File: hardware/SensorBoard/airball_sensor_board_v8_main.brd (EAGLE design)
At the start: 5.6 x 9.2 mm, 56 parts, among them IC1 CP2102, J2 USB Female Type C Connector, T1 BC846, T2 BC846, U1 BQ24075, U2 BQ27441-G1, U3 BMP388, U4 ESP-WROOM-32, U7 SP0503BAHT

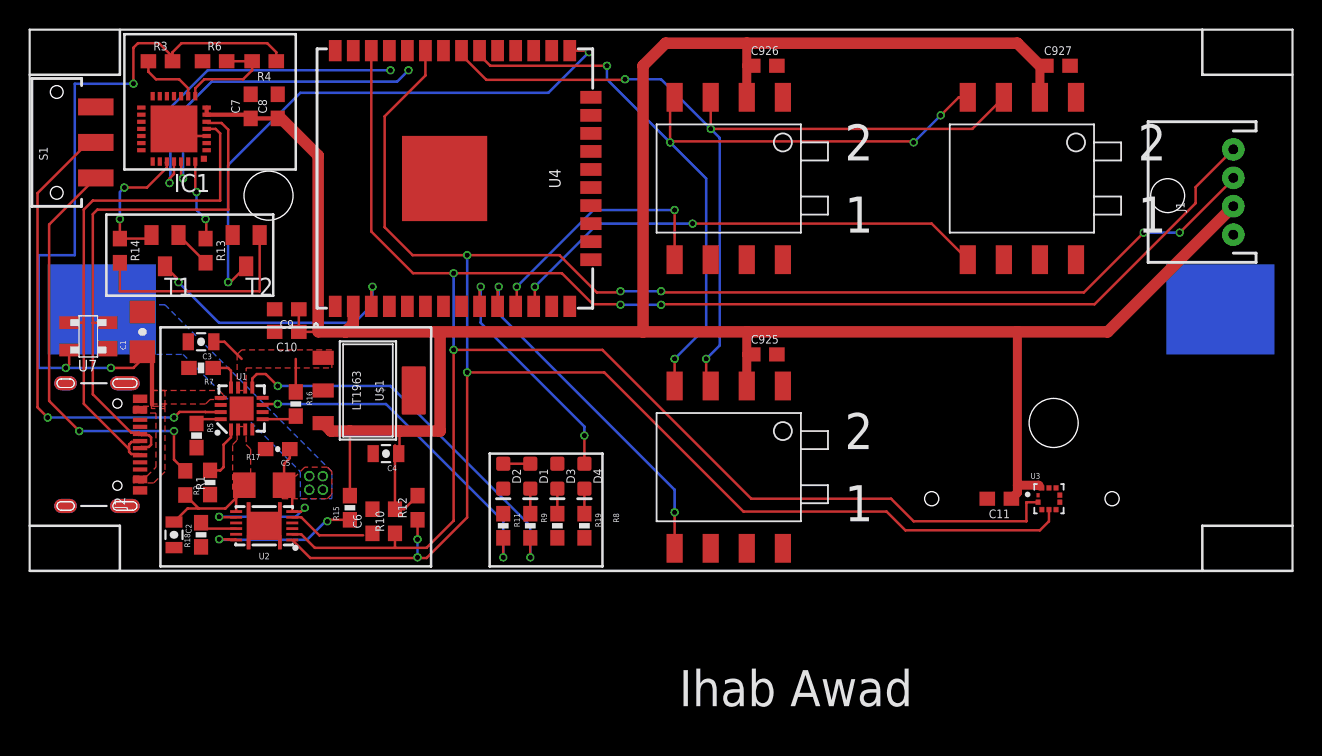
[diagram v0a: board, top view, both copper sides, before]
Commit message: More routing and documentation fixes.
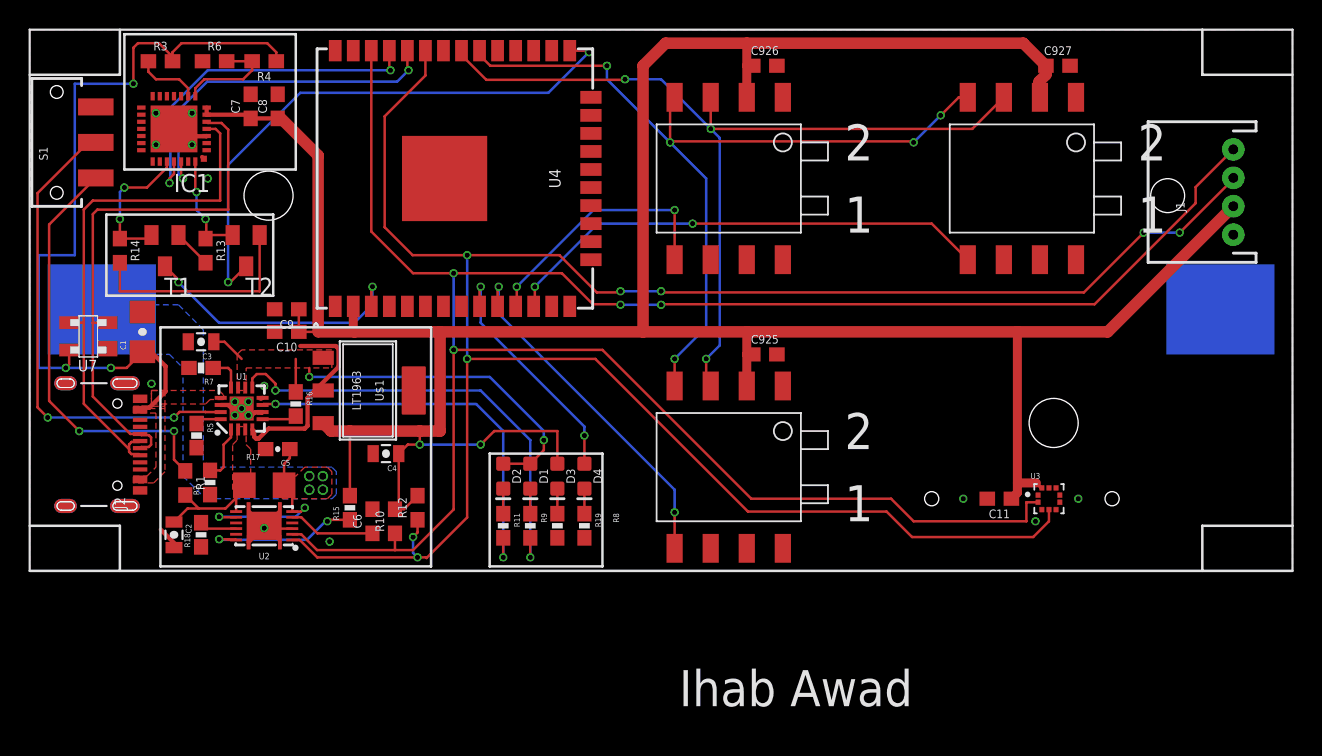
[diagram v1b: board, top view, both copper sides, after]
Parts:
- removed FRAME1, FRAME2: FRAME-LETTER, SparkFun-Aesthetics:CREATIVE_COMMONS
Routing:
- net GND: track 2.51 -> 34.5 mm, vias 0 -> 17
- net V_SUPPLY_UNREG: track 6.69 -> 28.1 mm, vias 0 -> 2
- net VCC: track 195.0 -> 209.0 mm, vias 0 -> 2
- net !CHG!: track 28.4 -> 32.2 mm
- net N$19: track 24.3 -> 28.0 mm
- net USB_TXD: track 23.1 -> 25.0 mm
- net N$20: track 0.00 -> 1.77 mm
- net USB_DTR: track 6.05 -> 7.70 mm
- net USB_RXD: track 23.6 -> 25.0 mm
- net SDA: track 160.5 -> 161.5 mm
- net N$14: track 5.52 -> 6.11 mm
- added copper zone on layer 1, net GND
- added copper zone on layer 16, net GND

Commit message: More routing fixes.
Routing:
- net GND: track 34.5 -> 19.6 mm
- net V_SUPPLY_UNREG: track 28.1 -> 29.2 mm, vias 2 -> 3
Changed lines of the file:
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@@
 <via x="14.9225" y="11.43" extent="1-16" drill="0.35"/>
 <via x="16.51" y="3.01625" extent="1-16" drill="0.35"/>
-<wire x1="16.3975" y1="11.18" x2="16.03095" y2="11.18" width="0.3048" layer="1"/>
 <via x="14.44625" y="11.90625" extent="1-16" drill="0.35"/>
 <via x="15.39875" y="11.90625" extent="1-16" drill="0.35"/>
@@
 <wire x1="15.639275" y1="10.95375" x2="15.39875" y2="10.95375" width="0.3048" layer="1"/>
 <wire x1="15.835725" y1="11.1502" x2="15.639275" y2="10.95375" width="0.3048" layer="1"/>
-<wire x1="14.9225" y1="11.43" x2="14.6427" y2="11.7098" width="0.3048" layer="1"/>
-<wire x1="14.009275" y1="11.6502" x2="14.705725" y2="10.95375" width="0.3048" layer="1"/>
 <wire x1="14.705725" y1="10.95375" x2="15.39875" y2="10.95375" width="0.3048" layer="1"/>
 <wire x1="10.542725" y1="1.5903" x2="9.2298" y2="2.903225" width="0.3048" layer="1"/>
@@
 <wire x1="16.3841" y1="12.1666" x2="16.2914" y2="12.1666" width="0.3048" layer="1"/>
 <wire x1="16.2914" y1="12.1666" x2="16.275" y2="12.1502" width="0.3048" layer="1"/>
-<wire x1="16.275" y1="12.1502" x2="16.1925" y2="12.1502" width="0.3048" layer="1"/>
 <via x="16.51" y="13.0175" extent="1-16" drill="0.35"/>
 <wire x1="15.41" y1="2.025" x2="16.430625" y2="3.045625" width="0.3048" layer="1"/>
 <wire x1="16.430625" y1="3.045625" x2="16.430625" y2="3.254375" width="0.3048" layer="1"/>
-<wire x1="15.8066" y1="9.43556875" x2="15.93306875" y2="9.3091" width="0.3048" layer="1"/>
-<wire x1="15.93306875" y1="9.3091" x2="16.11193125" y2="9.3091" width="0.3048" layer="1"/>
-<wire x1="19.369275" y1="10.0173" x2="19.5627" y2="10.210725" width="0.3048" layer="1"/>
-<wire x1="21.7427" y1="14.363225" x2="21.7427" y2="15.636775" width="0.3048" layer="1"/>
-<wire x1="21.7427" y1="15.636775" x2="21.549275" y2="15.8302" width="0.3048" layer="1"/>
-<wire x1="16.11193125" y1="9.3091" x2="16.82013125" y2="10.0173" width="0.3048" layer="1"/>
-<wire x1="16.82013125" y1="10.0173" x2="19.369275" y2="10.0173" width="0.3048" layer="1"/>
-<wire x1="19.5627" y1="10.210725" x2="19.5627" y2="12.183225" width="0.3048" layer="1"/>
-<wire x1="19.5627" y1="12.183225" x2="21.7427" y2="14.363225" width="0.3048" layer="1"/>
-<wire x1="15.6725" y1="9.955" x2="15.8066" y2="9.8209" width="0.3048" layer="1"/>
-<wire x1="15.8066" y1="9.8209" x2="15.8066" y2="9.43556875" width="0.3048" layer="1"/>
-<wire x1="14.402175" y1="11.7098" x2="15.158225" y2="10.95375" width="0.3048" layer="1"/>
 <wire x1="15.158225" y1="10.95375" x2="15.39875" y2="10.95375" width="0.3048" layer="1"/>
-<wire x1="21.549275" y1="15.8302" x2="19.0475" y2="15.8302" width="0.3048" layer="1"/>
+<wire x1="15.6725" y1="9.955" x2="15.6725" y2="10.43125" width="0.1778" layer="1"/>
+<wire x1="15.6725" y1="10.43125" x2="15.655459375" y2="10.414209375" width="0.1778" layer="1"/>
+<wire x1="14.9225" y1="11.14716875" x2="14.9225" y2="11.43" width="0.1778" layer="1"/>
+<wire x1="15.655459375" y1="10.414209375" x2="14.9225" y2="11.14716875" width="0.1778" layer="1"/>
 </signal>
 <signal name="V_USB">
@@
 <contactref element="U$1" pad="1"/>
 <contactref element="D2" pad="A"/>
-<wire x1="18.7325" y1="12.5975" x2="18.7325" y2="14.9225" width="0.1778" layer="1"/>
 <polygon width="0.1778" layer="1" thermals="no">
 <vertex x="14.605" y="12.7"/>
@@
 </polygon>
 <wire x1="35.2425" y1="7.5445" x2="33.3375" y2="7.5445" width="0.1778" layer="1"/>
-<wire x1="12.965" y1="16.129" x2="13.716" y2="16.129" width="0.1778" layer="1"/>
-<wire x1="13.716" y1="16.129" x2="14.9225" y2="14.9225" width="0.1778" layer="1"/>
-<via x="19.685" y="13.6525" extent="1-16" drill="0.35"/>
-<wire x1="19.685" y1="13.6525" x2="19.685" y2="14.2875" width="0.1778" layer="1"/>
-<wire x1="19.685" y1="13.6525" x2="32.385" y2="13.6525" width="0.1778" layer="16"/>
+<via x="19.05" y="14.9225" extent="1-16" drill="0.35"/>
+<wire x1="19.05" y1="14.9225" x2="20.32" y2="13.6525" width="0.1778" layer="16"/>
+<wire x1="32.385" y1="13.6525" x2="20.32" y2="13.6525" width="0.1778" layer="16"/>
 <wire x1="36.195" y1="9.8425" x2="32.385" y2="13.6525" width="0.1778" layer="16"/>
 <wire x1="36.195" y1="9.8425" x2="36.195" y2="9.2075" width="0.1778" layer="16"/>
@@
 <wire x1="36.195" y1="9.2075" x2="36.195" y2="8.497" width="0.1778" layer="1"/>
 <wire x1="36.195" y1="8.497" x2="35.2425" y2="7.5445" width="0.1778" layer="1"/>
+<wire x1="18.7325" y1="12.5975" x2="18.7325" y2="14.605" width="0.1778" layer="1"/>
+<wire x1="18.7325" y1="14.605" x2="19.05" y2="14.9225" width="0.1778" layer="1"/>
+<via x="15.39875" y="14.9225" extent="1-16" drill="0.35"/>
+<wire x1="12.965" y1="16.129" x2="14.19225" y2="16.129" width="0.1778" layer="1"/>
+<wire x1="14.19225" y1="16.129" x2="15.39875" y2="14.9225" width="0.1778" layer="1"/>
 </signal>
 <signal name="VCC">
